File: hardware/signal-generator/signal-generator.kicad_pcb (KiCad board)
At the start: 4 copper layers, 99.9 x 99.9 mm, 157 parts, among them J1 AVR-ISP-6, J10 Output_Conn, J11 SD_Card_Conn, J12 TP_Conn, J13 LCD_Conn, J2 AVR_SPI, J3 PORT_G, J4 PORT_F, J5 PORT_E, J6 PORT_A, J7 PORT_C, J8 AREF, J9 Power_Supply_Rails, Q1 MMBF5485, Q10 AP2310GN, Q11 AP2310GN, Q12 AP2310GN, Q2 MMBF5485, Q3 MMBF5485, Q4 AP2310GN, Q5 AP2310GN, Q6 AP2310GN, Q7 AP2310GN, Q8 AP2310GN, Q9 AP2310GN, SW1 RESET_BUTTON, U1 74HC04, U10 MCP23017-E/SO, U11 AD9764AR, U12 TS4061AICT-1.25, U13 74HC4040, U14 74HC4040, U15 MCP4551-103E/MS, U16 AD8021ARZ, U17 AD8021ARZ, U18 MCP4716, U19 AD8021ARZ, U2 74HC08, U20 MIC6211, U21 AZ431AN-A, U22 AD8021ARZ, U3 74HC08, U4 74HC30, U5 ATmega2561-16AU, U6 ADP7142AUJZ-5.0, U7 TC1017-3.3VCTTR, U8 DS1085Z-10+, U9 CY7C1021D-10ZSXI, Y1 16MHz

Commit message: [Signal Generator] Update names of internal PCB copper layers
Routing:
- added copper zone on Ground.Cu, net AGND
- removed copper zone on In2.Cu, net AGND

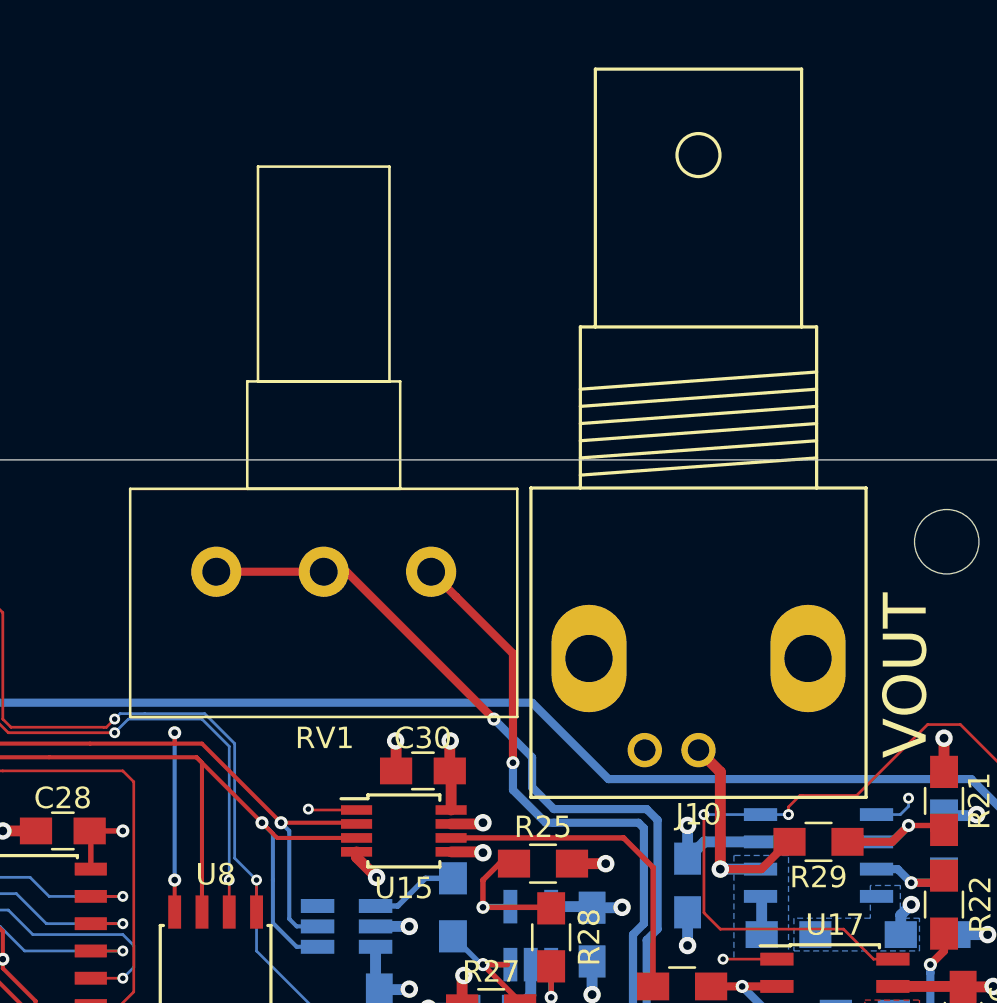
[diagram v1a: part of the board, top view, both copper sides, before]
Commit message: [Signal Generator] Slightly reposition output BNC and potentiometer PV1
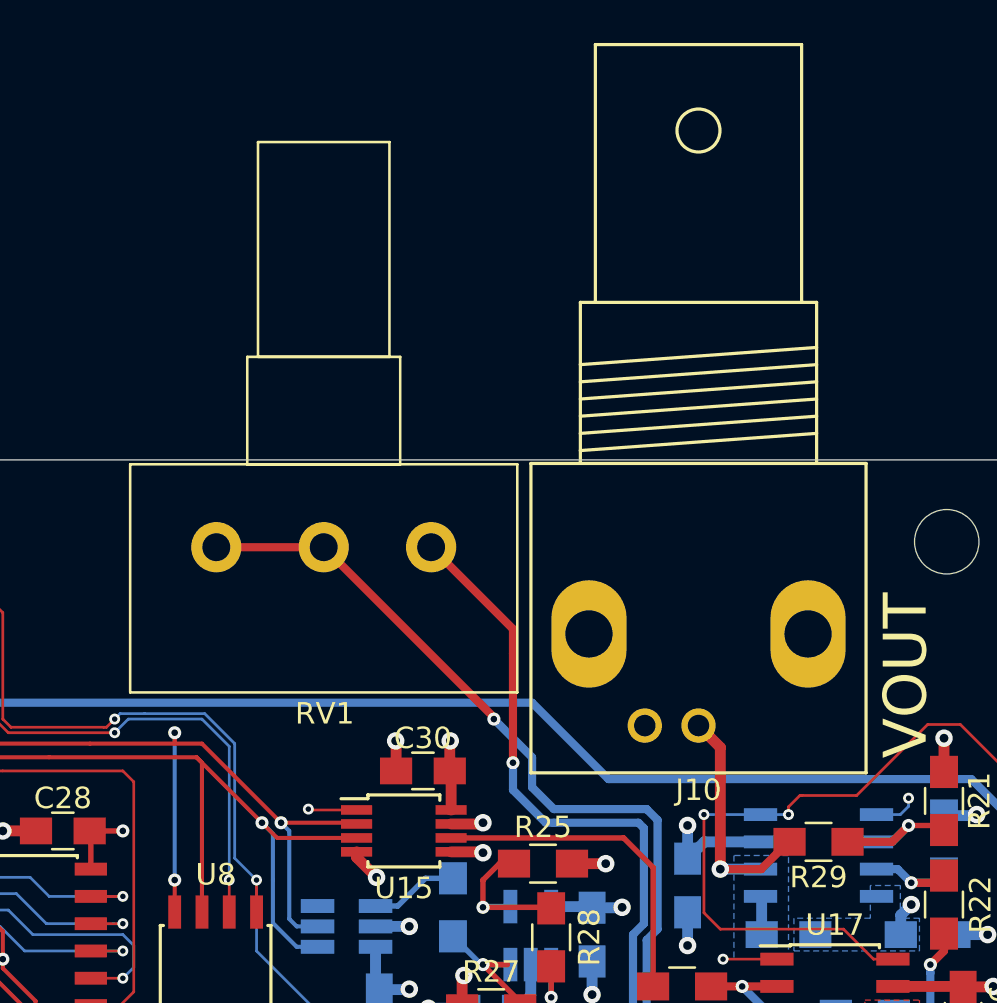
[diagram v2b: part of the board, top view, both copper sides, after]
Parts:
- moved RV1 1.14 mm to (174.6, 57.8)
- moved J10 1.14 mm to (187.1, 61.1)
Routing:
- net Net-(Q1-Pad1): track 54.8 -> 56.0 mm
- net /Output Circuitry/VOUT: track 11.6 -> 12.7 mm
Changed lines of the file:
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@@
     (thickness 1.6)
     (drawings 34)
-    (tracks 2756)
+    (tracks 2755)
     (zones 0)
     (modules 157)
@@
     (visible_elements FFFFFF7F)
     (pcbplotparams
-      (layerselection 0x010fc_ffffffff)
+      (layerselection 0x01cfc_ffffffff)
       (usegerberextensions false)
       (usegerberattributes false)
@@
       (outputformat 1)
       (mirror false)
-      (drillshape 1)
+      (drillshape 0)
       (scaleselection 1)
-      (outputdirectory ""))
+      (outputdirectory "gerber/"))
   )
   (net 0 "")
@@
   )
   (module Connectors_TE-Connectivity:BNC_Socket_TYCO-AMP (layer F.Cu)
-    (at 187.071 62.23)
+    (at 187.071 61.087)
     (descr "BNC Socket TYCO AMP")
     (tags "BNC Socket TYCO AMP")
@@
   )
   (module Potentiometers:Potentiometer_Alps_RK163_Single_Vertical (layer F.Cu)
-    (at 174.625 58.928 90)
+    (at 174.625 57.785 90)
     (descr "Potentiometer, vertically mounted, Omeg PC16PU, Omeg PC16PU, Omeg PC16PU, Vishay/Spectrol 248GJ/249GJ Single, Vishay/Spectrol 248GJ/249GJ Single, Vishay/Spectrol 248GJ/249GJ Single, Vishay/Spectrol 248GH/249GH Single, Vishay/Spectrol 148/149 Single, Vishay/Spectrol 148/149 Single, Vishay/Spectrol 148/149 Single, Vishay/Spectrol 148A/149A Single with mounting plates, Vishay/Spectrol 148/149 Double, Vishay/Spectrol 148A/149A Double with mounting plates, Piher PC-16 Single, Piher PC-16 Single, Piher PC-16 Single, Piher PC-16SV Single, Piher PC-16 Double, Piher PC-16 Triple, Piher T16H Single, Piher T16L Single, Piher T16H Double, Alps RK163 Single, http://www.alps.com/prod/info/E/PDF/Potentiometer/MetalShaft/RK163/RK163.PDF")
     (tags "Potentiometer vertical  Omeg PC16PU  Omeg PC16PU  Omeg PC16PU  Vishay/Spectrol 248GJ/249GJ Single  Vishay/Spectrol 248GJ/249GJ Single  Vishay/Spectrol 248GJ/249GJ Single  Vishay/Spectrol 248GH/249GH Single  Vishay/Spectrol 148/149 Single  Vishay/Spectrol 148/149 Single  Vishay/Spectrol 148/149 Single  Vishay/Spectrol 148A/149A Single with mounting plates  Vishay/Spectrol 148/149 Double  Vishay/Spectrol 148A/149A Double with mounting plates  Piher PC-16 Single  Piher PC-16 Single  Piher PC-16 Single  Piher PC-16SV Single  Piher PC-16 Double  Piher PC-16 Triple  Piher T16H Single  Piher T16L Single  Piher T16H Double  Alps RK163 Single")
@@
   (segment (start 189.992 72.771) (end 188.087 72.771) (width 0.381) (layer F.Cu) (net 54))
   (via (at 188.087 72.771) (size 0.8128) (drill 0.4064) (layers F.Cu B.Cu) (net 54))
-  (segment (start 188.087 68.24726) (end 187.071 67.23126) (width 0.508) (layer F.Cu) (net 54))
-  (segment (start 188.087 72.771) (end 188.087 68.24726) (width 0.508) (layer F.Cu) (net 54))
+  (segment (start 188.087 67.10426) (end 187.071 66.08826) (width 0.508) (layer F.Cu) (net 54))
+  (segment (start 188.087 72.771) (end 188.087 67.10426) (width 0.508) (layer F.Cu) (net 54))
   (segment (start 152.019 143.383) (end 151.972 143.383) (width 0.127) (layer F.Cu) (net 55))
   (segment (start 152.969 140.438) (end 152.969 142.433) (width 0.127) (layer F.Cu) (net 55))
@@
   (segment (start 179.324 67.611) (end 179.324 67.564) (width 0.381) (layer B.Cu) (net 172))
   (segment (start 179.324 67.564) (end 177.546 65.786) (width 0.381) (layer B.Cu) (net 172))
-  (segment (start 170.688 58.928) (end 170.641 58.928) (width 0.381) (layer F.Cu) (net 172))
-  (segment (start 164.625 58.928) (end 169.625 58.928) (width 0.381) (layer F.Cu) (net 172))
-  (segment (start 170.688 58.928) (end 169.625 58.928) (width 0.381) (layer F.Cu) (net 172))
-  (segment (start 177.546 65.786) (end 170.688 58.928) (width 0.381) (layer F.Cu) (net 172))
+  (segment (start 164.625 57.785) (end 169.625 57.785) (width 0.381) (layer F.Cu) (net 172))
+  (segment (start 177.546 65.706) (end 177.546 65.786) (width 0.381) (layer F.Cu) (net 172))
+  (segment (start 169.625 57.785) (end 177.546 65.706) (width 0.381) (layer F.Cu) (net 172))
   (segment (start 189.818 86.995) (end 190.627 87.804) (width 0.254) (layer B.Cu) (net 173))
   (segment (start 187.8 86.995) (end 186.309 86.995) (width 0.254) (layer F.Cu) (net 173))
@@
   (segment (start 179.959 70.612) (end 178.435 69.088) (width 0.381) (layer B.Cu) (net 182))
   (via (at 182.753 88.011) (size 0.6096) (drill 0.3048) (layers F.Cu B.Cu) (net 182))
-  (segment (start 174.625 58.928) (end 175.794999 60.097999) (width 0.381) (layer F.Cu) (net 182))
-  (segment (start 175.794999 60.097999) (end 178.435 62.738) (width 0.381) (layer F.Cu) (net 182))
   (via (at 178.435 67.818) (size 0.6096) (drill 0.3048) (layers F.Cu B.Cu) (net 182))
   (segment (start 178.435 69.088) (end 178.435 67.818) (width 0.381) (layer B.Cu) (net 182))
-  (segment (start 178.435 67.818) (end 178.435 62.738) (width 0.381) (layer F.Cu) (net 182))
+  (segment (start 178.435 62.738) (end 178.435 67.818) (width 0.381) (layer F.Cu) (net 182))
+  (segment (start 174.625 57.785) (end 178.435 61.595) (width 0.381) (layer F.Cu) (net 182))
+  (segment (start 178.435 61.595) (end 178.435 62.738) (width 0.381) (layer F.Cu) (net 182))
   (segment (start 128.651 144.907) (end 130.429 146.685) (width 0.127) (layer B.Cu) (net 183))
   (segment (start 110.236 128.143) (end 109.601 127.508) (width 0.127) (layer F.Cu) (net 183))
